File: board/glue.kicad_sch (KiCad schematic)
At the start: 2 parts, among them U12 PORTS

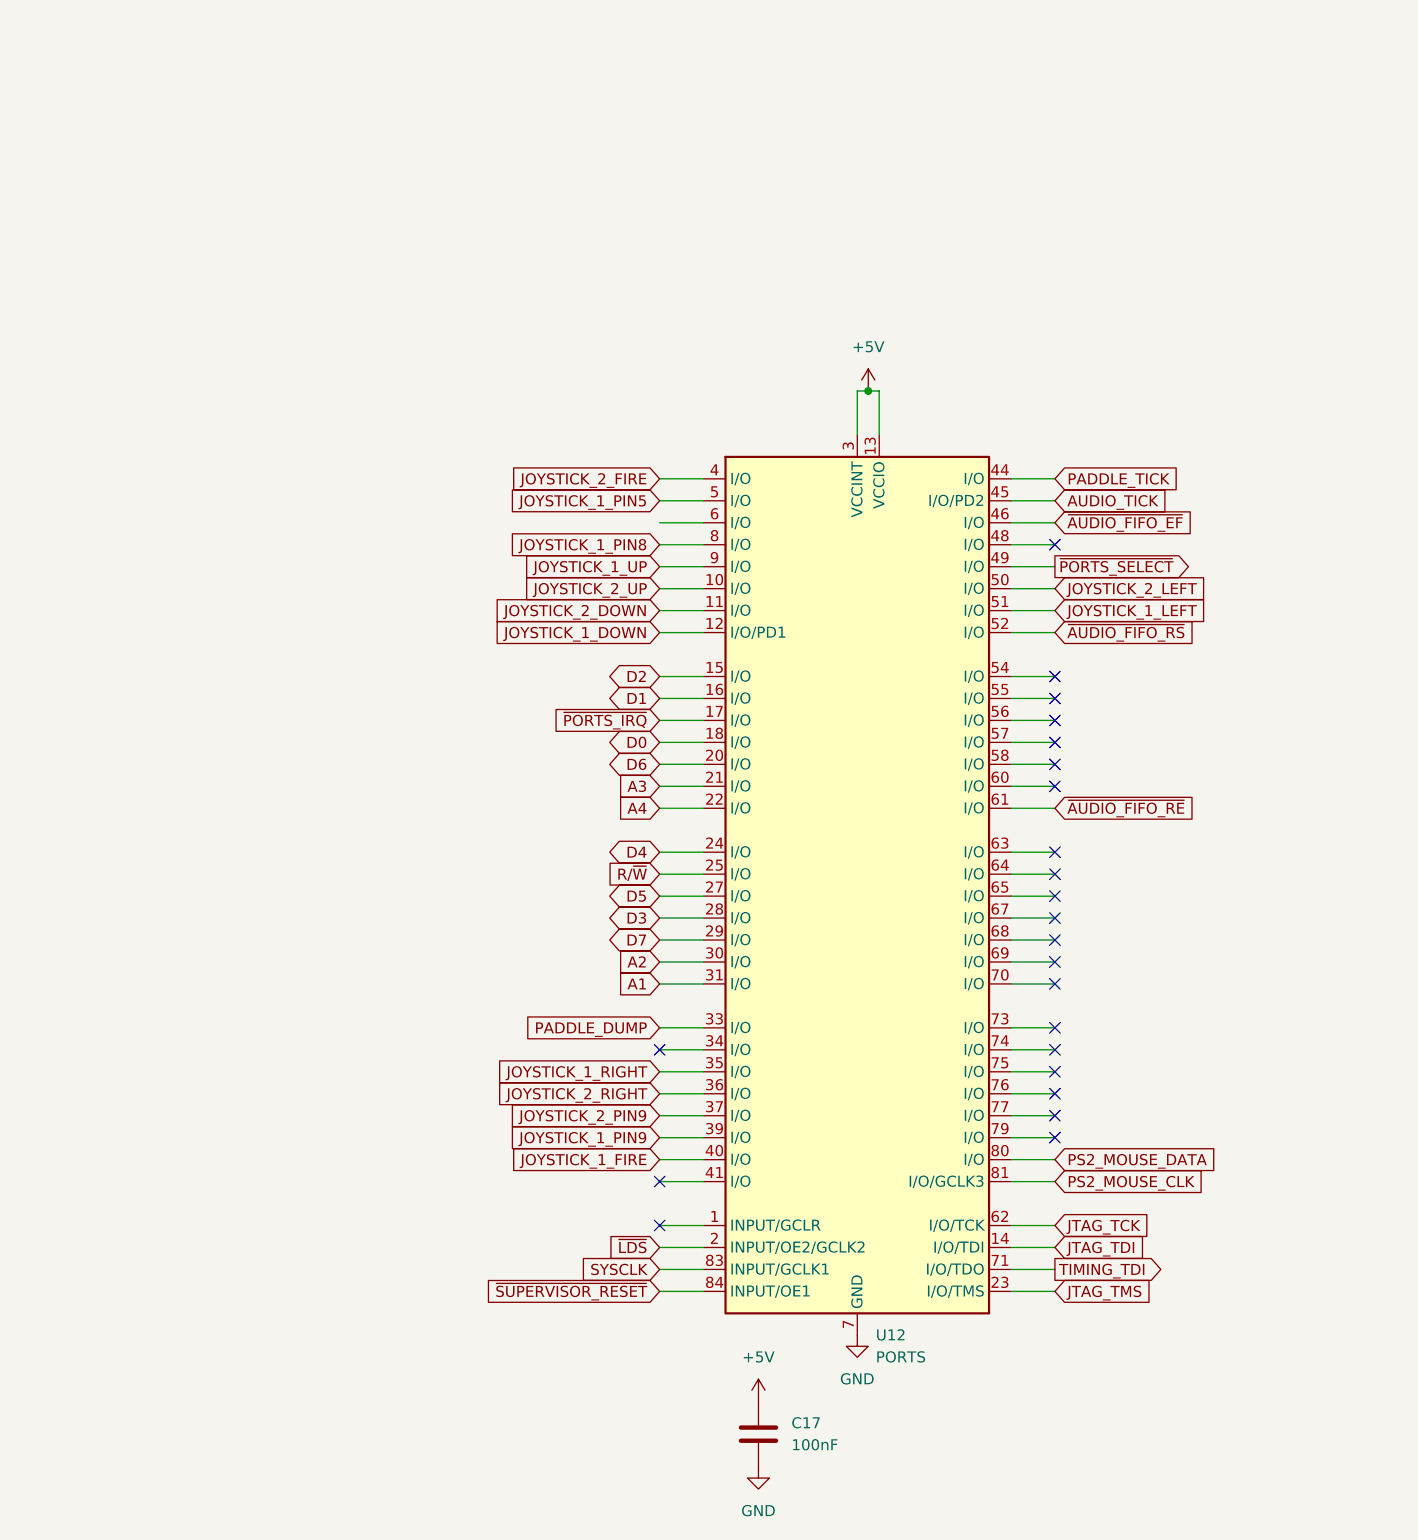
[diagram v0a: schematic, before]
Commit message: capture ENGINE in schematic; fix couple of shorts
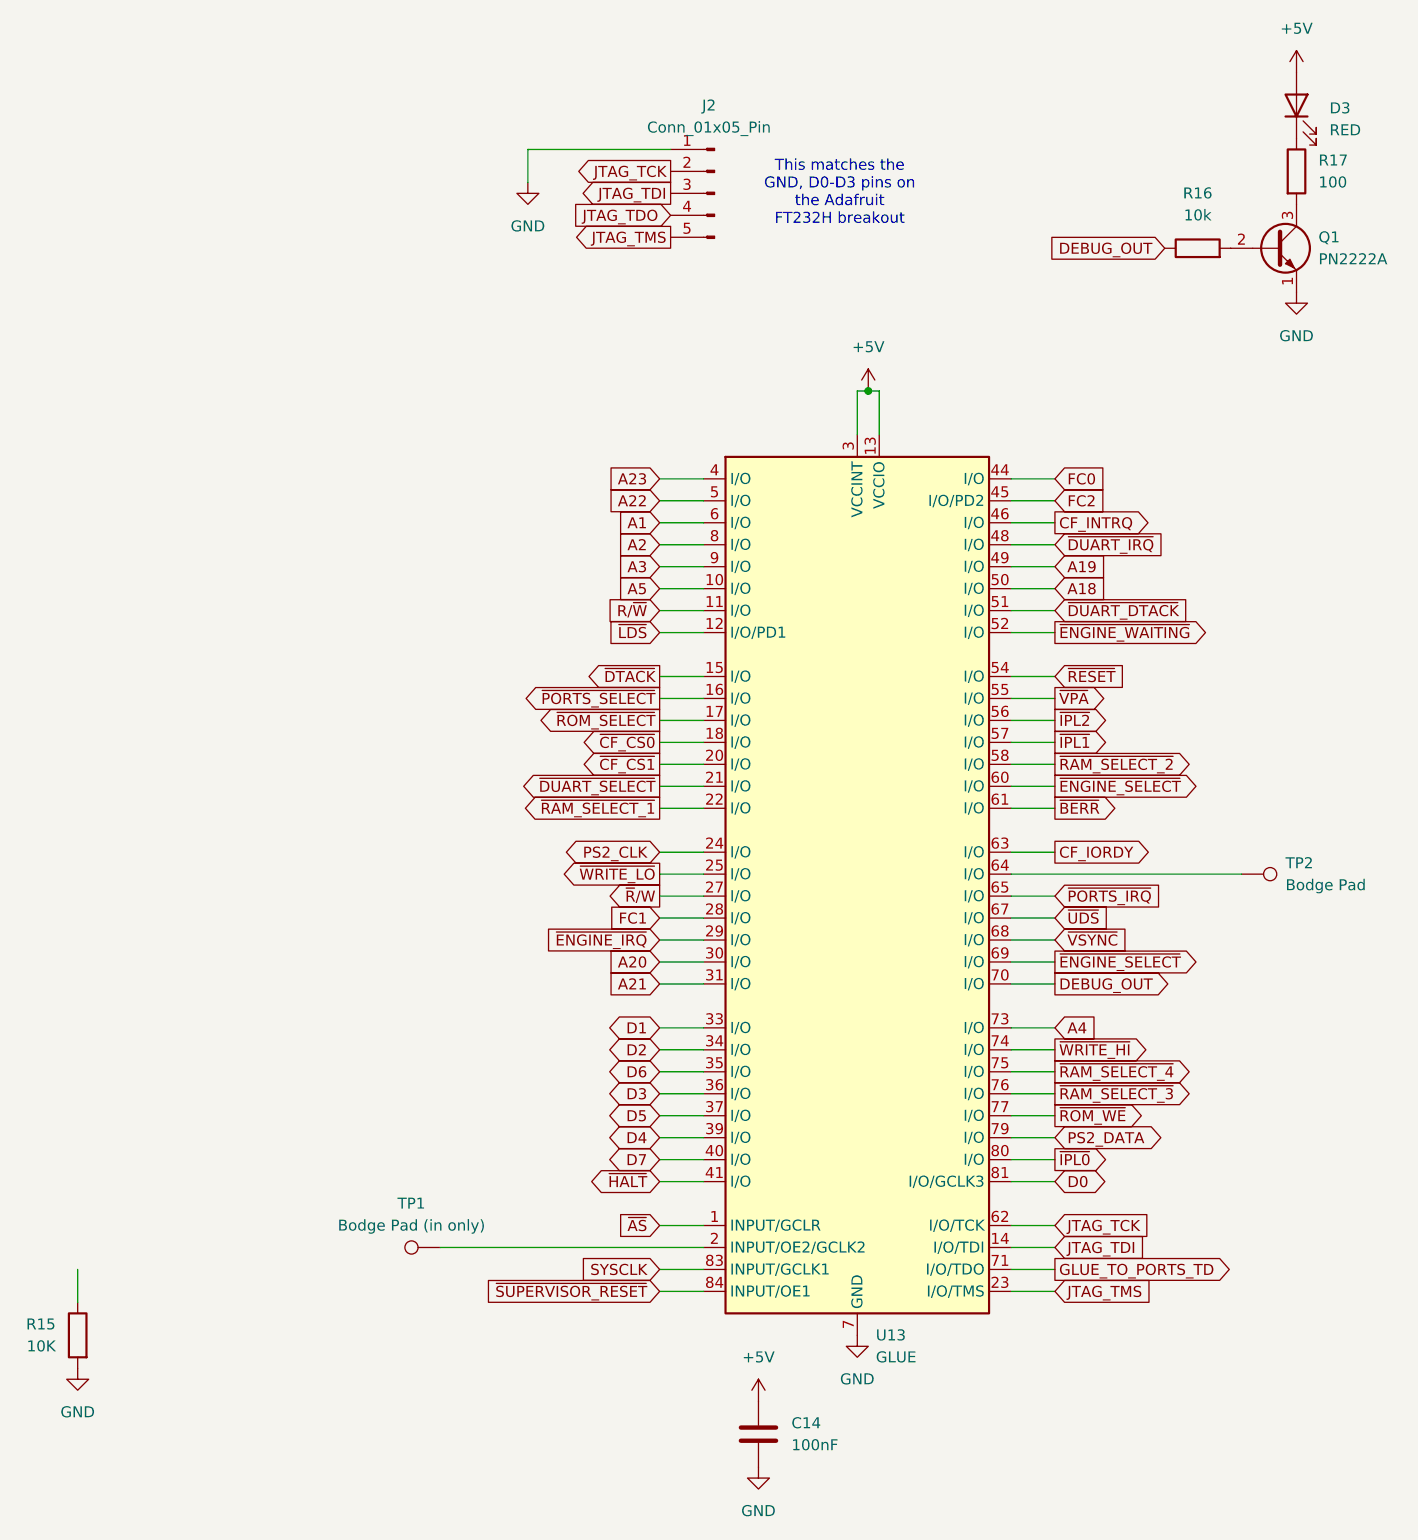
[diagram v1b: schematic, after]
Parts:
- added D3: RED, LED_THT:LED_D3.0mm, symbol Device:LED
- added J2: Conn_01x05_Pin, Connector_PinHeader_2.54mm:PinHeader_1x05_P2.54mm_Vertical, symbol Connector:Conn_01x05_Pin
- added Q1: PN2222A, Package_TO_SOT_THT:TO-92_Inline, symbol Transistor_BJT:PN2222A
- added R15: 10K, Resistor_THT:R_Axial_DIN0207_L6.3mm_D2.5mm_P10.16mm_Horizontal, symbol Device:R
- added R16: 10k, Resistor_THT:R_Axial_DIN0207_L6.3mm_D2.5mm_P10.16mm_Horizontal, symbol Device:R
- added R17: 100, Resistor_THT:R_Axial_DIN0207_L6.3mm_D2.5mm_P10.16mm_Horizontal, symbol Device:R
- added TP1: Bodge Pad (in only), symbol Connector:TestPoint
- added TP2: Bodge Pad, symbol Connector:TestPoint
- U13: renamed from U12; value PORTS -> GLUE
- renumbered C17 to C14
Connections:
- net JOYSTICK_1_DOWN is gone; now on net ~{LDS}: U13.12 (I/O/PD1)
- net JOYSTICK_1_FIRE is gone; now on net D7: U13.40 (I/O)
- net JOYSTICK_1_PIN8 is gone; now on net A2: U13.8 (I/O)
- net JOYSTICK_1_PIN9 is gone; now on net D4: U13.39 (I/O)
- net JOYSTICK_1_RIGHT is gone; now on net D6: U13.35 (I/O)
- net JOYSTICK_1_UP is gone; now on net A3: U13.9 (I/O)
- net JOYSTICK_2_DOWN is gone; now on net R/~{W}: U13.11 (I/O)
- net JOYSTICK_2_PIN9 is gone; now on net D5: U13.37 (I/O)
- net JOYSTICK_2_RIGHT is gone; now on net D3: U13.36 (I/O)
- net PADDLE_DUMP is gone; now on net D1: U13.33 (I/O)
- net PS2_MOUSE_CLK is gone; now on net D0: U13.81 (I/O/GCLK3)
- net +5V: now also D3.2 (A)
- net A1: now also U13.6 (I/O); no longer U13.31 (I/O)
- net A2: no longer U13.30 (I/O)
- net A3: no longer U13.21 (I/O)
- net A4: now also U13.73 (I/O); no longer U13.22 (I/O)
- net D0: no longer U13.18 (I/O)
- net D1: no longer U13.16 (I/O)
- net D2: now also U13.34 (I/O); no longer U13.15 (I/O)
- net D3: no longer U13.28 (I/O)
- net D4: no longer U13.24 (I/O)
- net D5: no longer U13.27 (I/O)
- net D6: no longer U13.20 (I/O)
- net D7: no longer U13.29 (I/O)
- net GND: now also J2.1 (Pin_1), Q1.1 (E), R15.2
- net JTAG_TCK: now also J2.2 (Pin_2)
- net JTAG_TDI: now also J2.3 (Pin_3)
- net JTAG_TMS: now also J2.5 (Pin_5)
- net R/~{W}: no longer U13.25 (I/O)
- net ~{LDS}: no longer U13.2 (INPUT/OE2/GCLK2)
- net ~{PORTS_IRQ}: now also U13.65 (I/O); no longer U13.17 (I/O)
- net ~{PORTS_SELECT}: now also U13.16 (I/O); no longer U13.49 (I/O)
- net ~{AS}: now reaches U13.1 (INPUT/GCLR)
- net ~{HALT}: now reaches U13.41 (I/O)
- net ~{DUART_IRQ}: now reaches U13.48 (I/O)
- net ~{RESET}: now reaches U13.54 (I/O)
- net ~{VPA}: now reaches U13.55 (I/O)
- net ~{IPL2}: now reaches U13.56 (I/O)
- net ~{IPL1}: now reaches U13.57 (I/O)
- net ~{RAM_SELECT_2}: now reaches U13.58 (I/O)
- net ~{ENGINE_SELECT}: now reaches U13.60 (I/O)
- net ~{ENGINE_SELECT}: now also U13.69 (I/O)
- net CF_IORDY: now reaches U13.63 (I/O)
- net at U13.64 (I/O): now also TP2.1
- net ~{UDS}: now reaches U13.67 (I/O)
- net ~{VSYNC}: now reaches U13.68 (I/O)
- net DEBUG_OUT: now reaches U13.70 (I/O)
- net DEBUG_OUT: now also R16.1
- net ~{WRITE_HI}: now reaches U13.74 (I/O)
- net ~{RAM_SELECT_4}: now reaches U13.75 (I/O)
- net ~{RAM_SELECT_3}: now reaches U13.76 (I/O)
- net ~{ROM_WE}: now reaches U13.77 (I/O)
- net PS2_DATA: now reaches U13.79 (I/O)
- net AUDIO_TICK renamed FC2
- net JOYSTICK_1_LEFT renamed ~{DUART_DTACK}
- net JOYSTICK_1_PIN5 renamed A22
- net JOYSTICK_2_FIRE renamed A23
- net JOYSTICK_2_LEFT renamed A18
- net JOYSTICK_2_UP renamed A5
- net PADDLE_TICK renamed FC0
- net PS2_MOUSE_DATA renamed ~{IPL0}
- net TIMING_TDI renamed GLUE_TO_PORTS_TD
- net ~{AUDIO_FIFO_EF} renamed CF_INTRQ
- net ~{AUDIO_FIFO_RE} renamed ~{BERR}
- net ~{AUDIO_FIFO_RS} renamed ~{ENGINE_WAITING}
- new net: Q1.2 (B), R16.2
- new net: TP1.1, U13.2 (INPUT/OE2/GCLK2)
- new net: D3.1 (K), R17.1
- new net: Q1.3 (C), R17.2
- new net A19: U13.49 (I/O)
- new net A20: U13.30 (I/O)
- new net A21: U13.31 (I/O)
- new net FC1: U13.28 (I/O)
- new net JTAG_TDO: J2.4 (Pin_4)
- new net PS2_CLK: U13.24 (I/O)
- new net ~{CF_CS0}: U13.18 (I/O)
- new net ~{CF_CS1}: U13.20 (I/O)
- new net ~{DTACK}: U13.15 (I/O)
- new net ~{DUART_SELECT}: U13.21 (I/O)
- new net ~{ENGINE_IRQ}: U13.29 (I/O)
- new net ~{RAM_SELECT_1}: U13.22 (I/O)
- new net ~{ROM_SELECT}: U13.17 (I/O)
- new net ~{R}/W: U13.27 (I/O)
- new net ~{WRITE_LO}: U13.25 (I/O)
- no-connect marks 23 -> 0
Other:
- note added: "This matches the GND, D0-D3 pins on the Adafruit FT232H breakout"

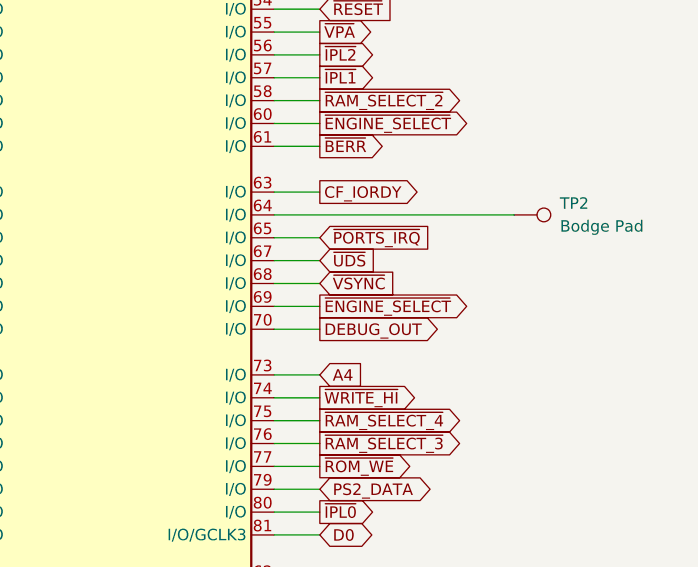
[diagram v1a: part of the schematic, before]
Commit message: capture TIMING; add PLCC44 ATF1504; a few fixes
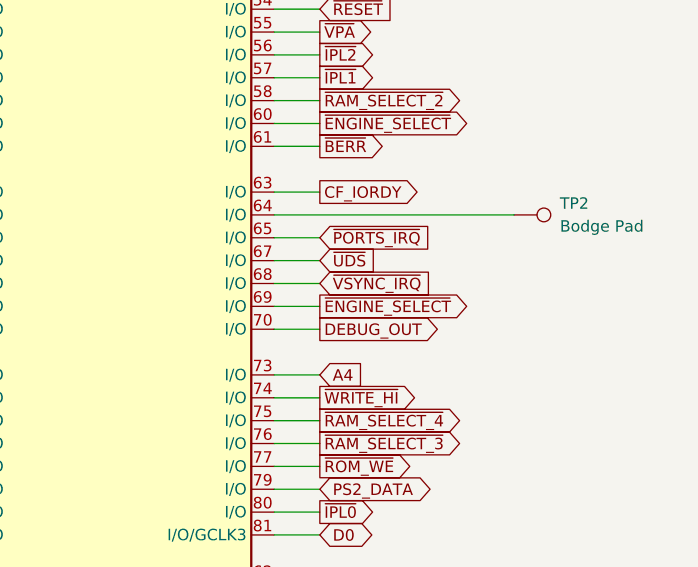
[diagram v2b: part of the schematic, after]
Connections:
- net ~{VSYNC} renamed ~{VSYNC_IRQ}
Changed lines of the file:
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@@
 		)
 	)
-	(global_label "~{VSYNC}"
+	(global_label "~{VSYNC_IRQ}"
 		(shape input)
 		(at 118.11 128.27 0)

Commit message: checkpoint CPLDs
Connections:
- net ~{ENGINE_SELECT}: no longer U13.69 (I/O)
- net at TP1.1, U13.2 (INPUT/OE2/GCLK2): now also R15.1
- net ~{ENGINE_WAITING} renamed ENGINE_WAITING
- new net ENGINE_ACTIVE: U13.69 (I/O)
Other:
- moved on the sheet: R15
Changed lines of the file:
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@@
 	)
 	(junction
+		(at 46.99 163.83)
+		(diameter 0)
+		(color 0 0 0 0)
+	)
+	(junction
 		(at 96.52 64.77)
 		(diameter 0)
@@
 	(wire
 		(pts
-			(xy 5.08 170.18) (xy 5.08 166.37)
+			(xy 46.99 167.64) (xy 46.99 163.83)
 		)
 		(stroke
@@
 		)
 	)
-	(global_label "~{ENGINE_SELECT}"
-		(shape output)
+	(global_label "ENGINE_ACTIVE"
+		(shape input)
 		(at 118.11 130.81 0)
 		(fields_autoplaced yes)
@@
 		)
 		(property "Intersheetrefs" "${INTERSHEET_REFS}"
-			(at 135.6698 130.81 0)
+			(at 135.0652 130.81 0)
 			(effects
 				(font
@@
 		)
 	)
-	(global_label "~{ENGINE_WAITING}"
-		(shape output)
+	(global_label "ENGINE_WAITING"
+		(shape input)
 		(at 118.11 92.71 0)
 		(fields_autoplaced yes)
@@
 	(symbol
 		(lib_id "Device:R")
-		(at 5.08 173.99 0)
+		(at 46.99 171.45 0)
 		(mirror y)
 		(unit 1)
@@
 		(fields_autoplaced yes)
 		(property "Reference" "R15"
-			(at 2.54 172.7199 0)
+			(at 44.45 170.1799 0)
 			(effects
 				(font
@@
 		)
 		(property "Value" "10K"
-			(at 2.54 175.2599 0)
+			(at 44.45 172.7199 0)
 			(effects
 				(font
@@
 		)
 		(property "Footprint" "Resistor_THT:R_Axial_DIN0207_L6.3mm_D2.5mm_P10.16mm_Horizontal"
-			(at 6.858 173.99 90)
+			(at 48.768 171.45 90)
 			(effects
 				(font
@@
 		)
 		(property "Datasheet" "~"
-			(at 5.08 173.99 0)
+			(at 46.99 171.45 0)
 			(effects
 				(font
@@
 		)
 		(property "Description" "Resistor"
-			(at 5.08 173.99 0)
+			(at 46.99 171.45 0)
 			(effects
 				(font
@@
 	(symbol
 		(lib_id "power:GND")
-		(at 5.08 177.8 0)
+		(at 46.99 175.26 0)
 		(mirror y)
 		(unit 1)
@@
 		(fields_autoplaced yes)
 		(property "Reference" "#PWR082"
-			(at 5.08 184.15 0)
+			(at 46.99 181.61 0)
 			(effects
 				(font
@@
 		)
 		(property "Value" "GND"
-			(at 5.08 182.88 0)
+			(at 46.99 180.34 0)
 			(effects
 				(font
@@
 		)
 		(property "Footprint" ""
-			(at 5.08 177.8 0)
+			(at 46.99 175.26 0)
 			(effects
 				(font
@@
 		)
 		(property "Datasheet" ""
-			(at 5.08 177.8 0)
+			(at 46.99 175.26 0)
 			(effects
 				(font
@@
 		)
 		(property "Description" "Power symbol creates a global label with name \"GND\" , ground"
-			(at 5.08 177.8 0)
+			(at 46.99 175.26 0)
 			(effects
 				(font
